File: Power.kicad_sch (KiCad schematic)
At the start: 28 parts

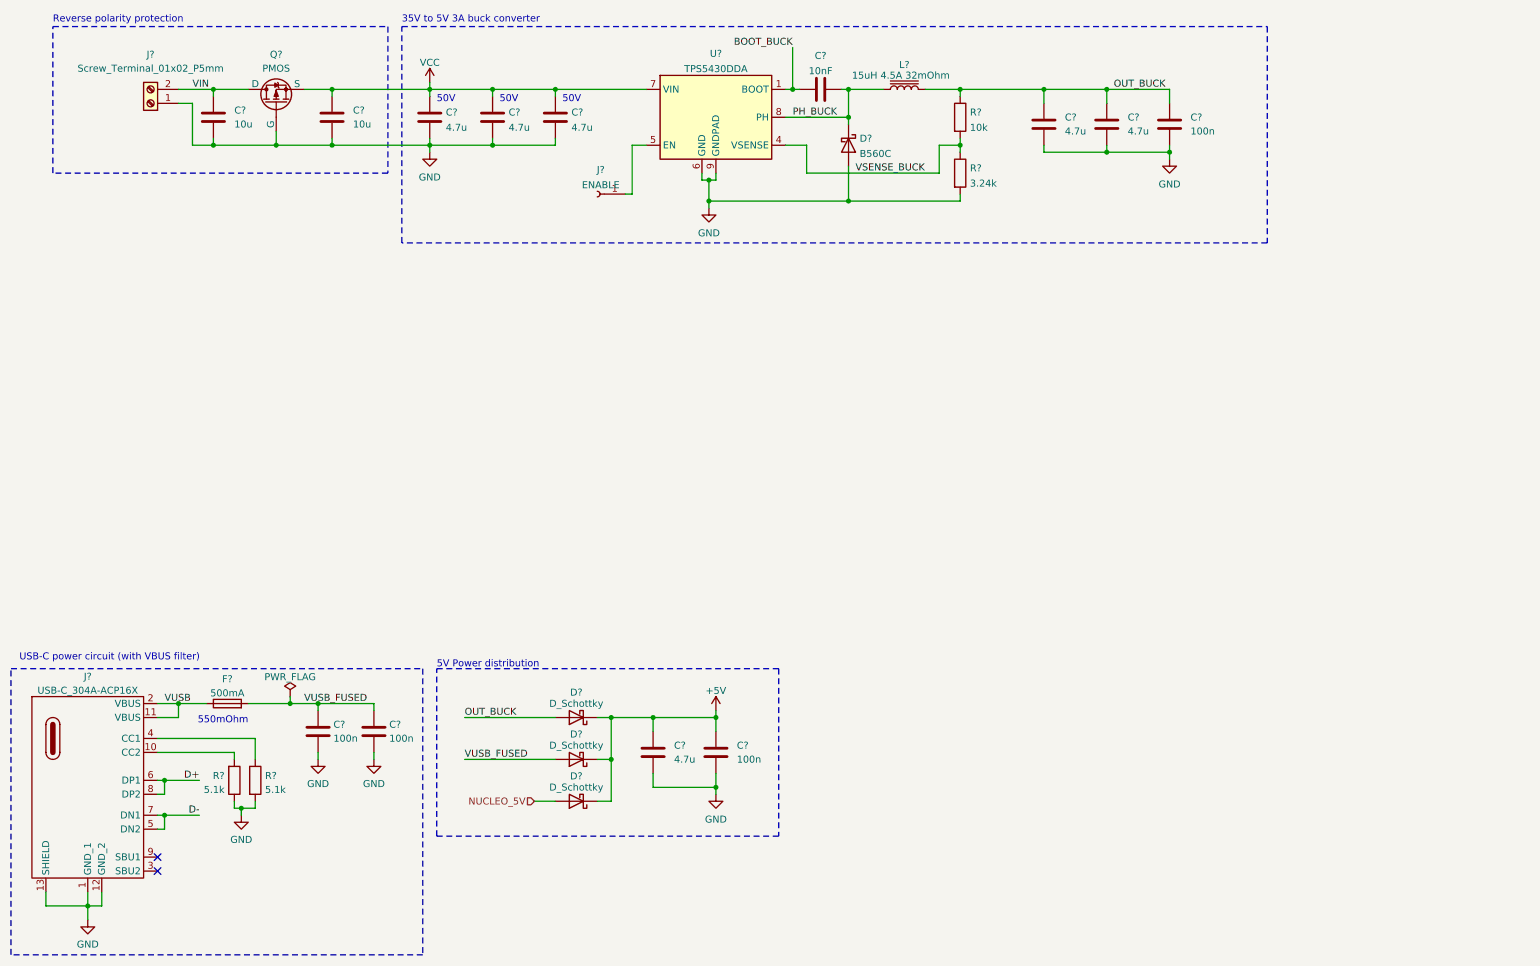
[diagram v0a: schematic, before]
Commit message: Connected the nucleo to local nets
 - I created all the local lables to the MCU schematic and connected them to the corresponding pins of the Nucleo board.
 - I renumed the hierarchical sheets to be in order of importance
 - I added solder jumpers for making the board more versatile in some cases
 - Corrected the Nucleo pinout on the schematic symbol
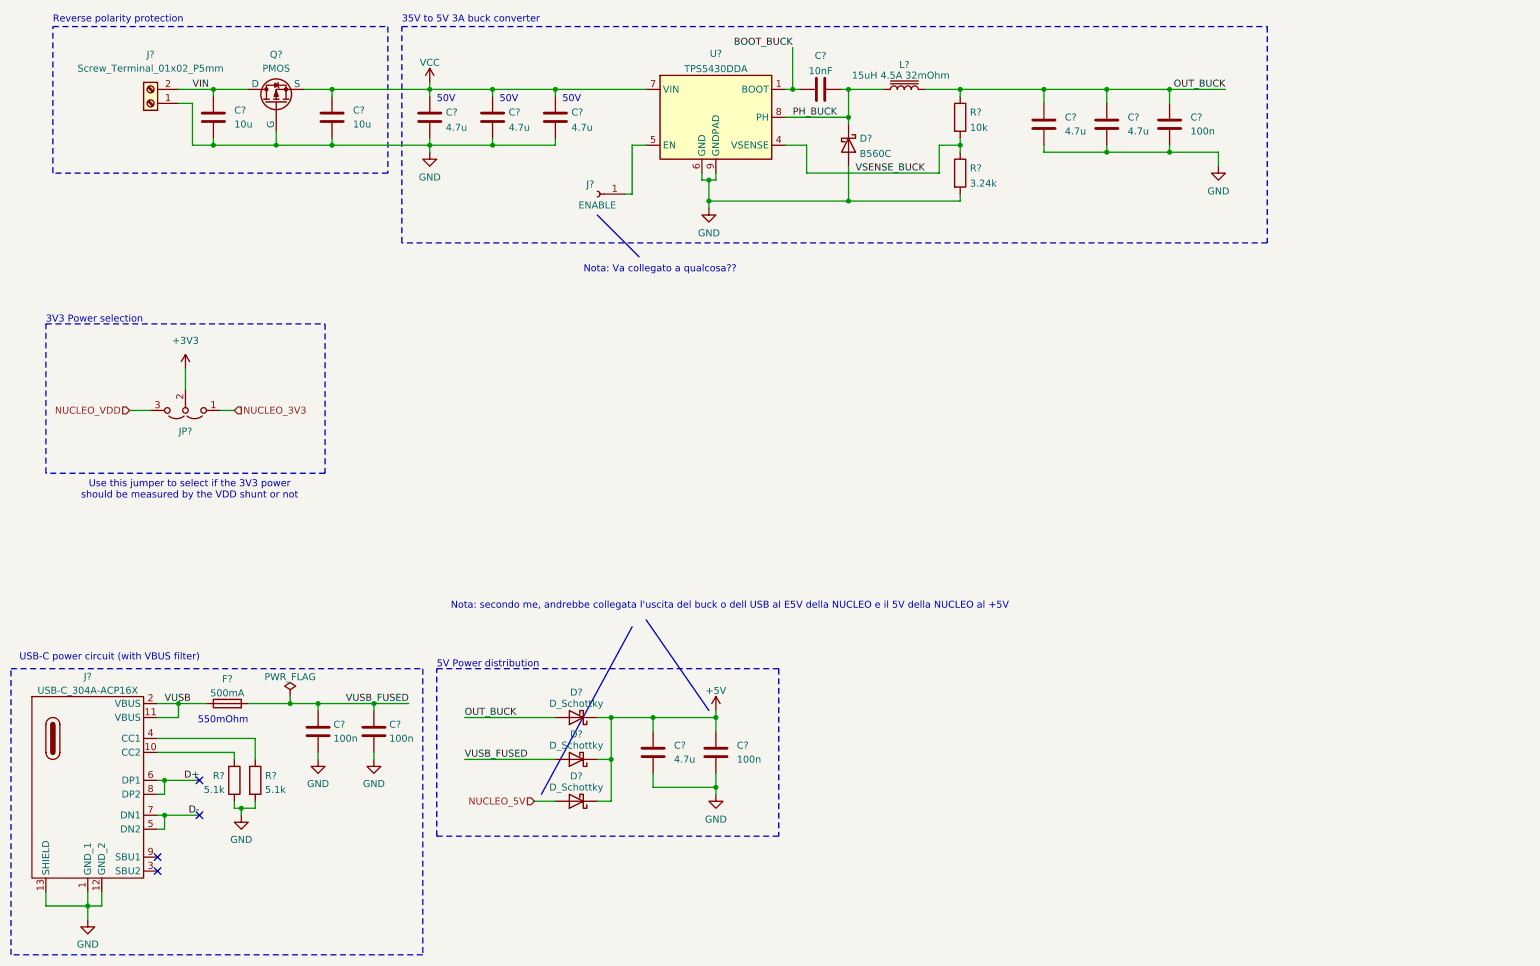
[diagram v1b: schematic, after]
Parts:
- added JP?: Jumper_3_Open, Connector_PinHeader_2.54mm:PinHeader_1x03_P2.54mm_Vertical, symbol Jumper:Jumper_3_Open
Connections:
- new net +3V3: JP?.2 (C)
- new net NUCLEO_3V3: JP?.1 (A)
- new net NUCLEO_VDD: JP?.3 (B)
- no-connect marks 2 -> 4
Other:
- note added: "3V3 Power selection"
- note added: "Nota: Va collegato a qualcosa??"
- note added: "Nota: secondo me, andrebbe collegata l'uscita del buck o dell USB al E5V della NUCLEO e il 5V della NUCLEO al +5V"
- note added: "Use this jumper to select if the 3V3 power should be measured by the VDD shunt or not"

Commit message: Small changes
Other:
- moved on the sheet: R?
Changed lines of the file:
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@@
+	)
+	(junction
+		(at 62.23 163.83)
+		(diameter 0)
+		(color 0 0 0 0)
 	)
 	(junction
@@
 	)
 	(junction
-		(at 60.96 163.83)
-		(diameter 0)
-		(color 0 0 0 0)
-	)
-	(junction
 		(at 229.87 44.45)
 		(diameter 0)
@@
 	(wire
 		(pts
-			(xy 60.96 163.83) (xy 60.96 165.1)
+			(xy 62.23 163.83) (xy 62.23 165.1)
 		)
 		(stroke
@@
 	(wire
 		(pts
-			(xy 45.72 151.13) (xy 63.5 151.13)
+			(xy 45.72 151.13) (xy 64.77 151.13)
 		)
 		(stroke
@@
 	(wire
 		(pts
-			(xy 59.69 163.83) (xy 60.96 163.83)
-		)
-		(stroke
-			(width 0)
-			(type default)
-		)
-	)
-	(wire
-		(pts
-			(xy 63.5 151.13) (xy 63.5 154.94)
+			(xy 59.69 163.83) (xy 62.23 163.83)
+		)
+		(stroke
+			(width 0)
+			(type default)
+		)
+	)
+	(wire
+		(pts
+			(xy 64.77 151.13) (xy 64.77 154.94)
 		)
 		(stroke
@@
 	(wire
 		(pts
-			(xy 63.5 163.83) (xy 60.96 163.83)
+			(xy 64.77 163.83) (xy 62.23 163.83)
 		)
 		(stroke
@@
 	(wire
 		(pts
-			(xy 63.5 162.56) (xy 63.5 163.83)
+			(xy 64.77 162.56) (xy 64.77 163.83)
 		)
 		(stroke
@@
 	(symbol
 		(lib_id "Device:R")
-		(at 63.5 158.75 0)
+		(at 64.77 158.75 0)
 		(unit 1)
 		(exclude_from_sim no)
@@
 		(fields_autoplaced yes)
 		(property "Reference" "R?"
-			(at 65.278 157.9153 0)
+			(at 66.548 157.9153 0)
 			(effects
 				(font
@@
 		)
 		(property "Value" "5.1k"
-			(at 65.278 160.4522 0)
+			(at 66.548 160.4522 0)
 			(effects
 				(font
@@
 		)
 		(property "Footprint" "Resistor_SMD:R_0805_2012Metric_Pad1.20x1.40mm_HandSolder"
-			(at 61.722 158.75 90)
+			(at 62.992 158.75 90)
 			(effects
 				(font
@@
 		)
 		(property "Datasheet" "~"
-			(at 63.5 158.75 0)
+			(at 64.77 158.75 0)
 			(effects
 				(font
@@
 		)
 		(property "Description" ""
-			(at 63.5 158.75 0)
+			(at 64.77 158.75 0)
 			(effects
 				(font
@@
 	(symbol
 		(lib_id "power:GND")
-		(at 60.96 165.1 0)
+		(at 62.23 165.1 0)
 		(unit 1)
 		(exclude_from_sim no)
@@
 		(fields_autoplaced yes)
 		(property "Reference" "#PWR?"
-			(at 60.96 171.45 0)
+			(at 62.23 171.45 0)
 			(effects
 				(font
@@
 		)
 		(property "Value" "GND"
-			(at 60.96 169.5434 0)
+			(at 62.23 169.5434 0)
 			(effects
 				(font
@@
 		)
 		(property "Footprint" ""
-			(at 60.96 165.1 0)
+			(at 62.23 165.1 0)
 			(effects
 				(font
@@
 		)
 		(property "Datasheet" ""
-			(at 60.96 165.1 0)
+			(at 62.23 165.1 0)
 			(effects
 				(font
@@
 		)
 		(property "Description" ""
-			(at 60.96 165.1 0)
-			(effects
-				(font
+			(at 62.23 165.1 0)
+			(effects
+				(font

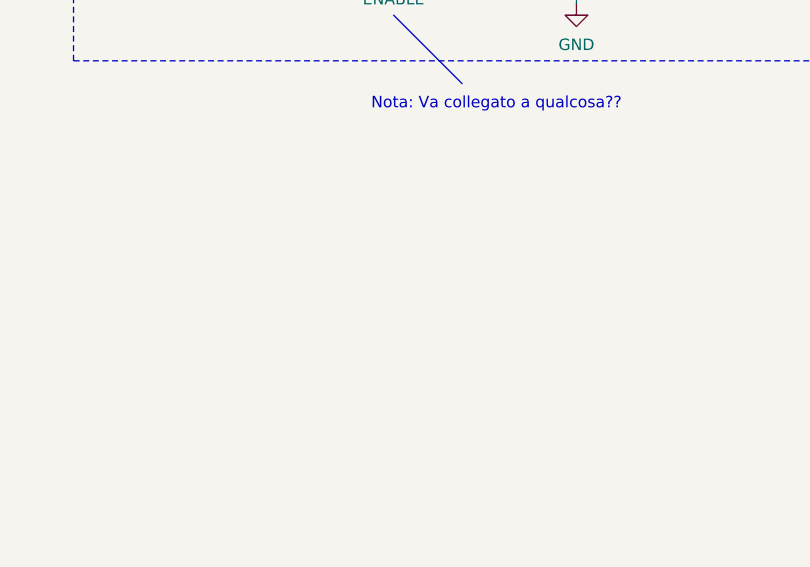
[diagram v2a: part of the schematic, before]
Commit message: Added Power connector of the nucleo to the schematic
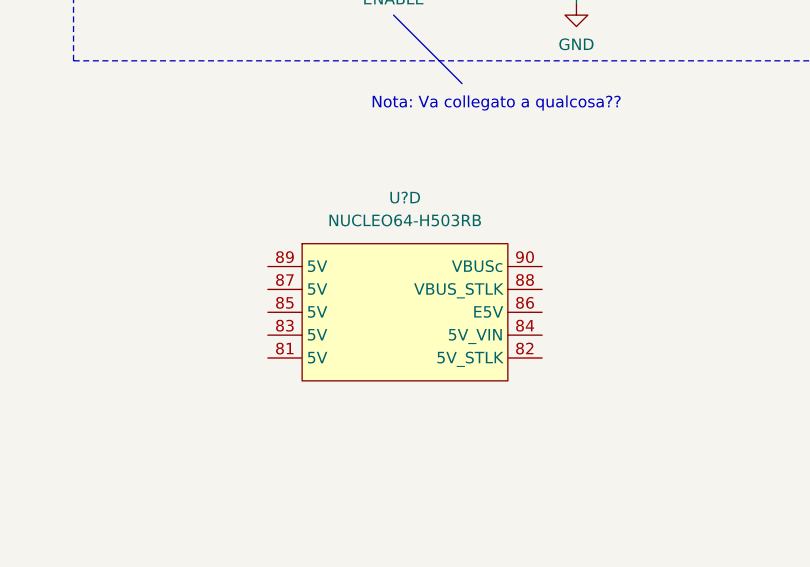
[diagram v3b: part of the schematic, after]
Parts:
- added U?: NUCLEO64-H503RB, ProjectConnectors:Nucleo64, symbol ProjectMCUs:NUCLEO64-H503RB

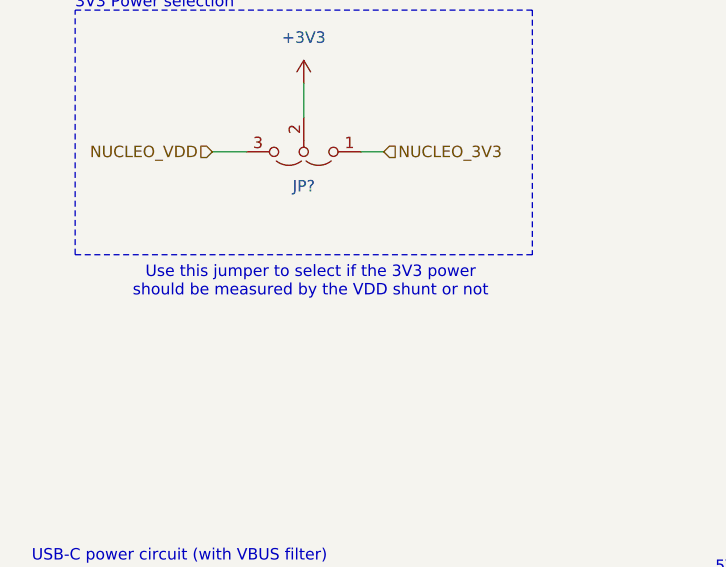
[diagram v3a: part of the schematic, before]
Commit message: Added the hierarchical pins of the sheets and connected them, Fixes #7
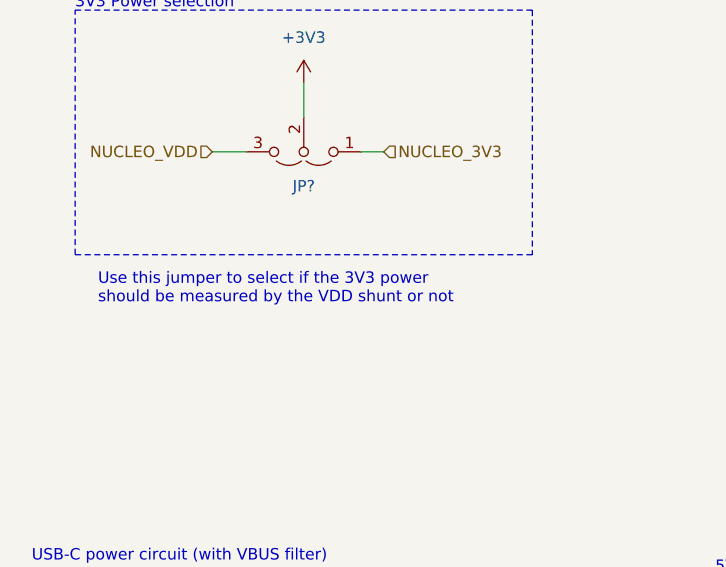
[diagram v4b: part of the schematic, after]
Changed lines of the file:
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@@
 	(text "Use this jumper to select if the 3V3 power \nshould be measured by the VDD shunt or not"
 		(exclude_from_sim no)
-		(at 51.562 105.918 0)
+		(at 27.94 106.68 0)
 		(effects
 			(font
 				(size 1.27 1.27)
 			)
+			(justify left)
 		)
 	)

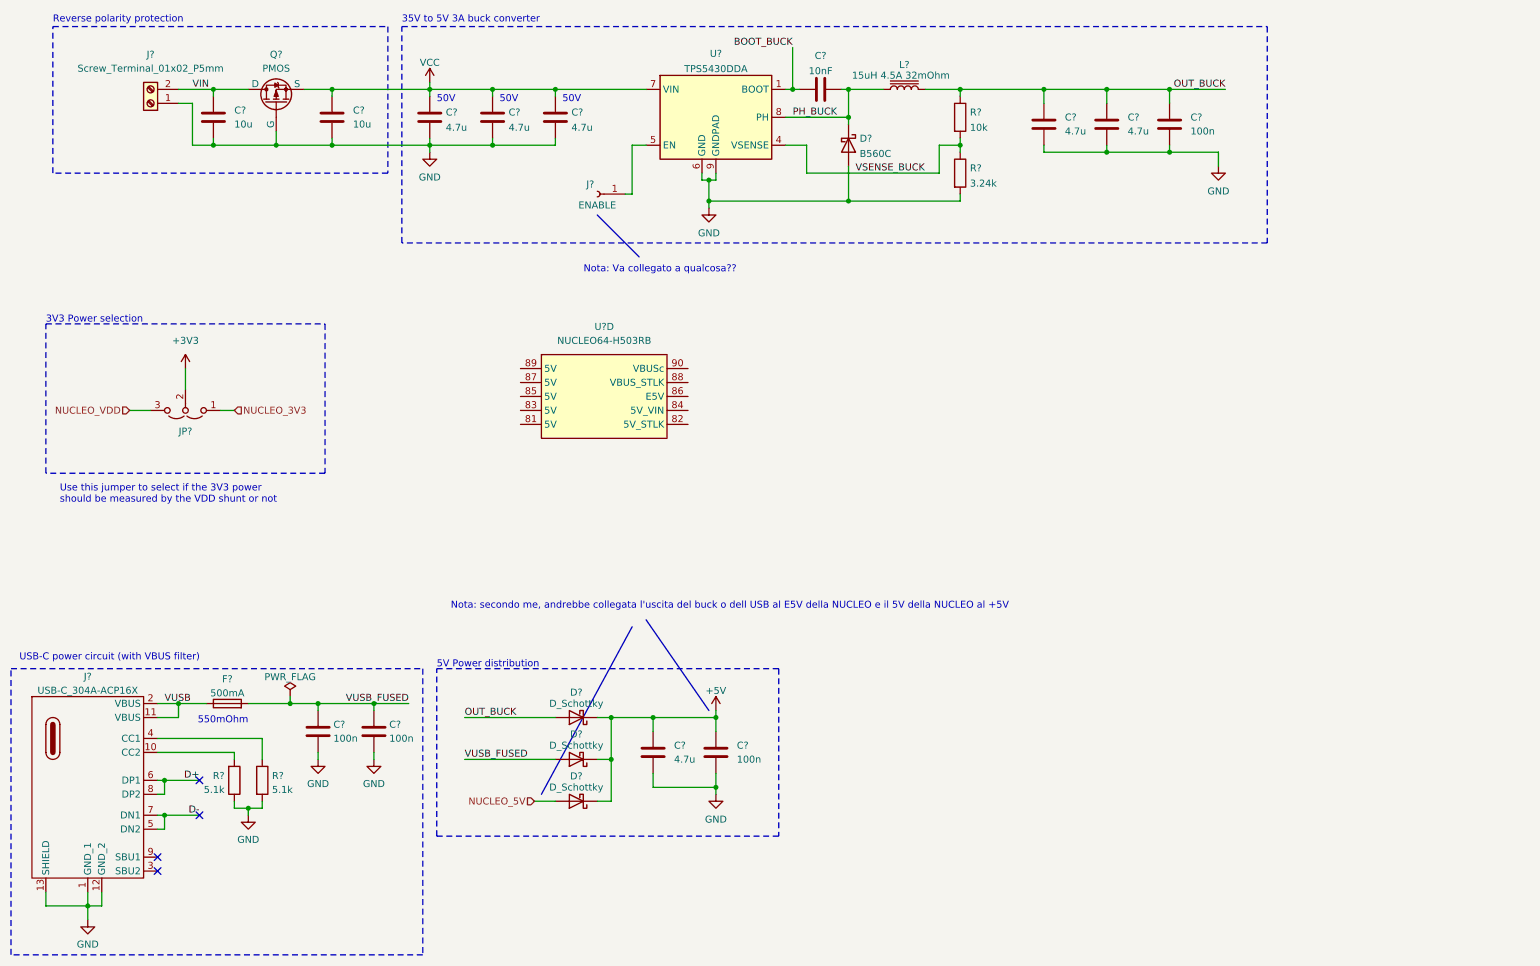
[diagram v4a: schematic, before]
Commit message: fixed #1 , added protection circuit 5V selector jumper
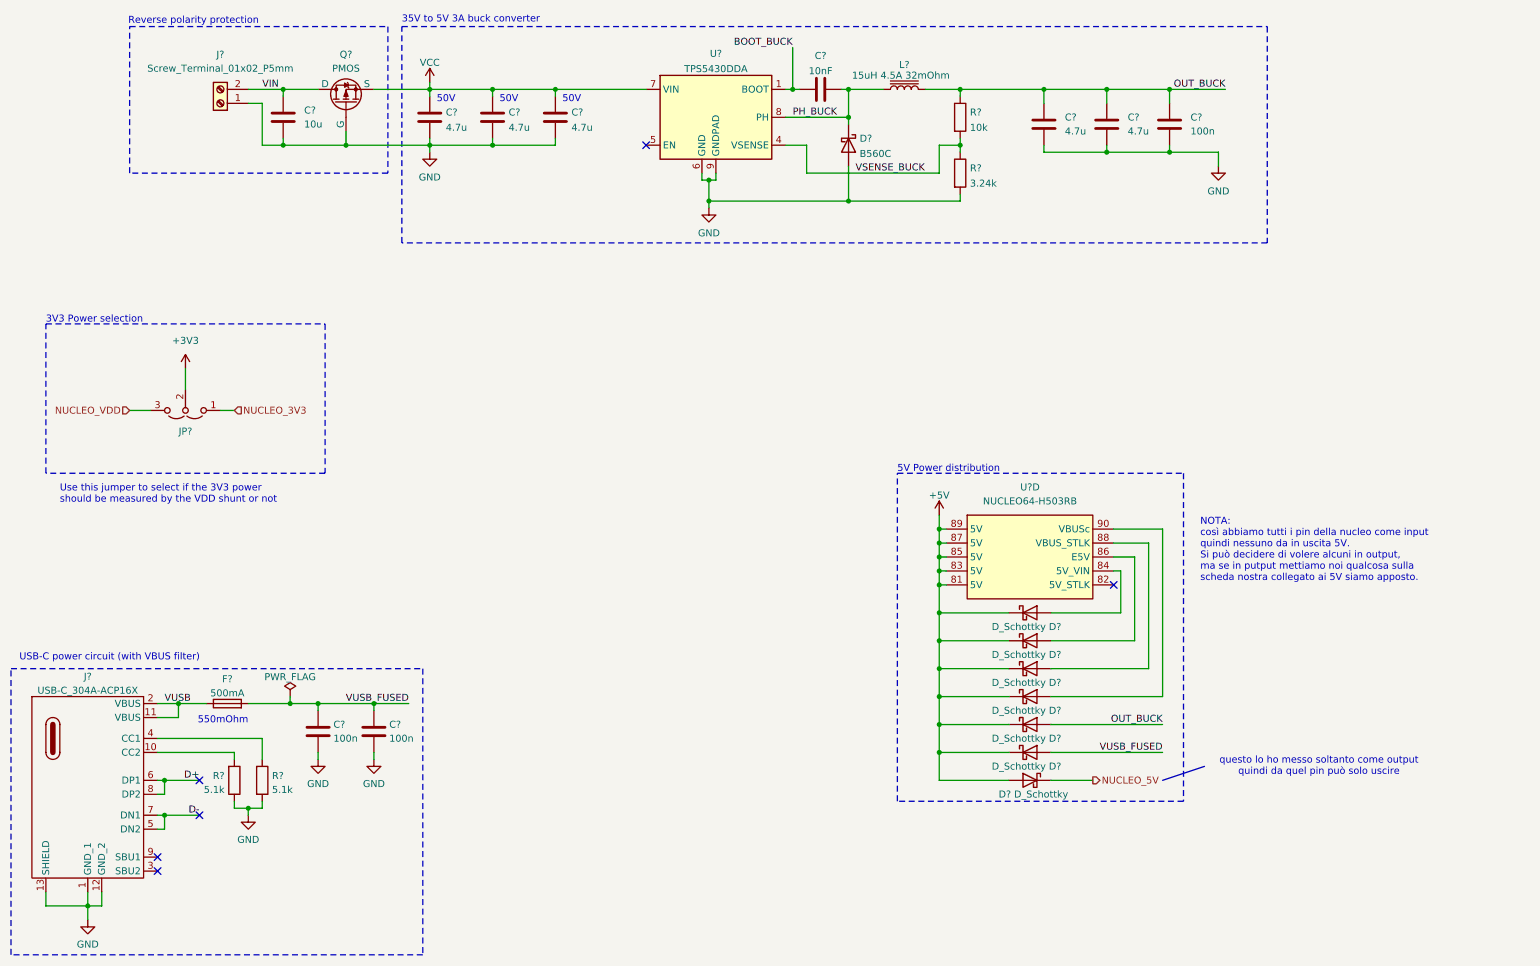
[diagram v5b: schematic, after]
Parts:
- removed C?: 10u, Capacitor_SMD:C_0805_2012Metric_Pad1.18x1.45mm_HandSolder, symbol Device:C
- removed C?: 4.7u, Capacitor_SMD:C_0805_2012Metric_Pad1.18x1.45mm_HandSolder, symbol Device:C
- removed C?: 100n, Capacitor_SMD:C_0805_2012Metric_Pad1.18x1.45mm_HandSolder, symbol Device:C
- removed D? (x3): D_Schottky, symbol Device:D_Schottky
- removed J?: ENABLE, Connector_PinHeader_2.54mm:PinHeader_1x01_P2.54mm_Vertical, symbol Connector:Conn_01x01_Female
- added D? (x7): D_Schottky, symbol Device:D_Schottky
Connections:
- net +5V: now also U?.81 (5V), U?.83 (5V), U?.85 (5V), U?.87 (5V), U?.89 (5V), D?.1 (K), D?.1 (K), D?.1 (K), D?.1 (K), D?.1 (K), D?.1 (K), D?.2 (A)
- net NUCLEO_5V: now also D?.1 (K)
- net OUT_BUCK: now also D?.2 (A)
- net VUSB_FUSED: now also D?.2 (A)
- net at U?.84 (5V_VIN): now also D?.2 (A)
- net at U?.86 (E5V): now also D?.2 (A)
- net at U?.88 (VBUS_STLK): now also D?.2 (A)
- net at U?.90 (VBUSc): now also D?.2 (A)
- no-connect marks 4 -> 6
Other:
- note added: "NOTA: così abbiamo tutti i pin della nucleo come input quindi nessuno da in uscita 5V. Si può decidere di volere alcuni in output, ma se in putput mettiamo noi qualcosa sulla scheda nostra collegato ai 5V siamo apposto."
- note added: "questo lo ho messo soltanto come output quindi da quel pin può solo uscire"
- note removed: "Nota: Va collegato a qualcosa??"
- note removed: "Nota: secondo me, andrebbe collegata l'uscita del buck o dell USB al E5V della NUCLEO e il 5V della NUCLEO al +5V"
- moved on the sheet: C?, J?, Q?, U?D
